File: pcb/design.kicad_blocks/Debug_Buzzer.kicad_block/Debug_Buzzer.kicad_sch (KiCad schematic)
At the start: 5 parts, among them Q1 S8050

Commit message: Rough layout of footprints for `VehicleFlightComputer`.
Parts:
- Q1: footprint Package_TO_SOT_THT:TO-92_Inline -> Package_TO_SOT_SMD:SOT-23_Handsoldering
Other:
- note added: "Debug Buzzer (V6 : SMD Footprint)."
- note removed: "Debug Buzzer (V5 : AST only)."
- moved on the sheet: BZ1, JP2, Q1, R15, R17
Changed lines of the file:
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@@
 	(rectangle
 		(start 461.137 241.681)
-		(end 541.02 284.48)
+		(end 551.18 284.48)
 		(stroke
 			(width 0.8128)
@@
 		)
 	)
-	(text "Debug Buzzer (V5 : AST only)."
+	(text "Debug Buzzer (V6 : SMD Footprint)."
 		(exclude_from_sim no)
 		(at 461.01 240.03 0)
@@
 	)
 	(junction
-		(at 501.65 266.7)
+		(at 506.73 266.7)
 		(diameter 0)
 		(color 0 0 0 0)
@@
 	(wire
 		(pts
-			(xy 501.65 260.35) (xy 499.11 260.35)
-		)
-		(stroke
-			(width 0)
-			(type default)
-		)
-	)
-	(wire
-		(pts
-			(xy 509.27 254) (xy 509.27 251.46)
-		)
-		(stroke
-			(width 0)
-			(type default)
-		)
-	)
-	(wire
-		(pts
-			(xy 491.49 260.35) (xy 488.95 260.35)
-		)
-		(stroke
-			(width 0)
-			(type default)
-		)
-	)
-	(wire
-		(pts
-			(xy 501.65 260.35) (xy 501.65 266.7)
-		)
-		(stroke
-			(width 0)
-			(type default)
-		)
-	)
-	(wire
-		(pts
-			(xy 491.49 273.05) (xy 488.95 273.05)
-		)
-		(stroke
-			(width 0)
-			(type default)
-		)
-	)
-	(wire
-		(pts
-			(xy 501.65 273.05) (xy 499.11 273.05)
-		)
-		(stroke
-			(width 0)
-			(type default)
-		)
-	)
-	(wire
-		(pts
-			(xy 509.27 259.08) (xy 509.27 261.62)
-		)
-		(stroke
-			(width 0)
-			(type default)
-		)
-	)
-	(wire
-		(pts
-			(xy 501.65 266.7) (xy 501.65 273.05)
+			(xy 506.73 260.35) (xy 504.19 260.35)
+		)
+		(stroke
+			(width 0)
+			(type default)
+		)
+	)
+	(wire
+		(pts
+			(xy 514.35 254) (xy 514.35 251.46)
+		)
+		(stroke
+			(width 0)
+			(type default)
+		)
+	)
+	(wire
+		(pts
+			(xy 496.57 260.35) (xy 494.03 260.35)
+		)
+		(stroke
+			(width 0)
+			(type default)
+		)
+	)
+	(wire
+		(pts
+			(xy 506.73 260.35) (xy 506.73 266.7)
+		)
+		(stroke
+			(width 0)
+			(type default)
+		)
+	)
+	(wire
+		(pts
+			(xy 496.57 273.05) (xy 494.03 273.05)
+		)
+		(stroke
+			(width 0)
+			(type default)
+		)
+	)
+	(wire
+		(pts
+			(xy 506.73 273.05) (xy 504.19 273.05)
+		)
+		(stroke
+			(width 0)
+			(type default)
+		)
+	)
+	(wire
+		(pts
+			(xy 514.35 259.08) (xy 514.35 261.62)
+		)
+		(stroke
+			(width 0)
+			(type default)
+		)
+	)
+	(wire
+		(pts
+			(xy 506.73 266.7) (xy 506.73 273.05)
 		)
 		(stroke
@@
 	(global_label "buzzer"
 		(shape bidirectional)
-		(at 485.14 266.7 180)
+		(at 490.22 266.7 180)
 		(fields_autoplaced yes)
 		(effects
@@
 		)
 		(property "Intersheetrefs" "${INTERSHEET_REFS}"
-			(at 474.8145 266.7 0)
+			(at 479.8945 266.7 0)
 			(effects
 				(font
@@
 	(symbol
 		(lib_id "power:GND")
-		(at 509.27 271.78 0)
+		(at 514.35 271.78 0)
 		(unit 1)
 		(exclude_from_sim no)
@@
 		(fields_autoplaced yes)
 		(property "Reference" "#PWR038"
-			(at 509.27 278.13 0)
+			(at 514.35 278.13 0)
 			(effects
 				(font
@@
 		)
 		(property "Value" "GND"
-			(at 509.2701 275.59 90)
+			(at 514.3501 275.59 90)
 			(effects
 				(font
@@
 		)
 		(property "Footprint" ""
-			(at 509.27 271.78 0)
+			(at 514.35 271.78 0)
 			(effects
 				(font
@@
 		)
 		(property "Datasheet" ""
-			(at 509.27 271.78 0)
+			(at 514.35 271.78 0)
 			(effects
 				(font
@@
 		)
 		(property "Description" "Power symbol creates a global label with name \"GND\" , ground"
-			(at 509.27 271.78 0)
+			(at 514.35 271.78 0)
 			(effects
 				(font
@@
 	(symbol
 		(lib_id "Jumper:Jumper_3_Bridged12")
-		(at 488.95 266.7 270)
+		(at 494.03 266.7 270)
 		(mirror x)
 		(unit 1)
@@
 		(fields_autoplaced yes)
 		(property "Reference" "JP2"
-			(at 491.49 266.6999 90)
+			(at 496.57 266.6999 90)
 			(effects
 				(font
@@
 		)
 		(property "Value" "Jumper_3_Bridged12"
-			(at 491.49 267.9699 90)
+			(at 496.57 267.9699 90)
 			(effects
 				(font
@@
 		)
 		(property "Footprint" "Connector_PinHeader_2.54mm:PinHeader_1x03_P2.54mm_Vertical"
-			(at 488.95 266.7 0)
+			(at 494.03 266.7 0)
 			(effects
 				(font
@@
 		)
 		(property "Datasheet" "~"
-			(at 488.95 266.7 0)
+			(at 494.03 266.7 0)
 			(effects
 				(font
@@
 		)
 		(property "Description" "Jumper, 3-pole, pins 1+2 closed/bridged"
-			(at 488.95 266.7 0)
+			(at 494.03 266.7 0)
 			(effects
 				(font
@@
 	(symbol
 		(lib_id "power:+3.3V")
-		(at 509.27 251.46 0)
+		(at 514.35 251.46 0)
 		(unit 1)
 		(exclude_from_sim no)
@@
 		(fields_autoplaced yes)
 		(property "Reference" "#PWR034"
-			(at 509.27 255.27 0)
+			(at 514.35 255.27 0)
 			(effects
 				(font
@@
 		)
 		(property "Value" "+3.3V"
-			(at 509.27 246.38 0)
+			(at 514.35 246.38 0)
 			(effects
 				(font
@@
 		)
 		(property "Footprint" ""
-			(at 509.27 251.46 0)
+			(at 514.35 251.46 0)
 			(effects
 				(font
@@
 		)
 		(property "Datasheet" ""
-			(at 509.27 251.46 0)
+			(at 514.35 251.46 0)
 			(effects
 				(font
@@
 		)
 		(property "Description" "Power symbol creates a global label with name \"+3.3V\""
-			(at 509.27 251.46 0)
+			(at 514.35 251.46 0)
 			(effects
 				(font
@@
 	(symbol
 		(lib_id "Device:R")
-		(at 495.3 260.35 90)
+		(at 500.38 260.35 90)
 		(unit 1)
 		(exclude_from_sim no)
@@
 		(fields_autoplaced yes)
 		(property "Reference" "R15"
-			(at 495.3 254 90)
+			(at 500.38 254 90)
 			(effects
 				(font
@@
 		)
 		(property "Value" "50k"
-			(at 495.3 256.54 90)
+			(at 500.38 256.54 90)
 			(effects
 				(font
@@
 		)
 		(property "Footprint" "Resistor_SMD:R_1206_3216Metric_Pad1.30x1.75mm_HandSolder"
-			(at 495.3 262.128 90)
+			(at 500.38 262.128 90)
 			(effects
 				(font
@@
 		)
 		(property "Datasheet" "~"
-			(at 495.3 260.35 0)
+			(at 500.38 260.35 0)
 			(effects
 				(font
@@
 		)
 		(property "Description" "Resistor"
-			(at 495.3 260.35 0)
+			(at 500.38 260.35 0)
 			(effects
 				(font
@@
 	(symbol
 		(lib_id "Transistor_BJT:S8050")
-		(at 506.73 266.7 0)
+		(at 511.81 266.7 0)
 		(unit 1)
 		(exclude_from_sim no)
@@
 		(fields_autoplaced yes)
 		(property "Reference" "Q1"
-			(at 511.81 265.4299 0)
+			(at 516.89 265.4299 0)
 			(effects
 				(font
@@
 		)
 		(property "Value" "S8050"
-			(at 511.81 267.9699 0)
-			(effects
-				(font
-					(size 1.27 1.27)
-				)
-				(justify left)
-			)
-		)
-		(property "Footprint" "Package_TO_SOT_THT:TO-92_Inline"
-			(at 511.81 268.605 0)
+			(at 516.89 267.9699 0)
+			(effects
+				(font
+					(size 1.27 1.27)
+				)
+				(justify left)
+			)
+		)
+		(property "Footprint" "Package_TO_SOT_SMD:SOT-23_Handsoldering"
+			(at 516.89 268.605 0)
 			(effects
 				(font
@@
 		)
 		(property "Datasheet" "http://www.unisonic.com.tw/datasheet/S8050.pdf"
-			(at 506.73 266.7 0)
+			(at 511.81 266.7 0)
 			(effects
 				(font
@@
 		)
 		(property "Description" "0.7A Ic, 20V Vce, Low Voltage High Current NPN Transistor, TO-92"
-			(at 506.73 266.7 0)
+			(at 511.81 266.7 0)
 			(effects
 				(font
@@
 	(symbol
 		(lib_id "Device:Buzzer")
-		(at 511.81 256.54 0)
+		(at 516.89 256.54 0)
 		(unit 1)
 		(exclude_from_sim no)
@@
 		(dnp no)
 		(property "Reference" "BZ1"
-			(at 515.62 255.2699 0)
+			(at 520.7 255.2699 0)
 			(effects
 				(font
@@
 		)
 		(property "Value" "AST1109MLTRQ"
-			(at 515.62 257.8099 0)
+			(at 520.7 257.8099 0)
 			(effects
 				(font
@@
 		)
 		(property "Footprint" "Buzzer_Beeper:Buzzer_Mallory_AST1109MLTRQ"
-			(at 511.175 254 90)
+			(at 516.255 254 90)
 			(effects
 				(font
@@
 		)
 		(property "Datasheet" "~"
-			(at 511.175 254 90)
+			(at 516.255 254 90)
 			(effects
 				(font
@@
 		)
 		(property "Description" "Buzzer, polarized"
-			(at 511.81 256.54 0)
+			(at 516.89 256.54 0)
 			(effects
 				(font
@@
 	(symbol
 		(lib_id "Device:R")
-		(at 495.3 273.05 90)
+		(at 500.38 273.05 90)
 		(unit 1)
 		(exclude_from_sim no)
@@
 		(dnp no)
 		(property "Reference" "R17"
-			(at 495.3 279.4 90)
+			(at 500.38 279.4 90)
 			(effects
 				(font
@@
 		)
 		(property "Value" "10k"
-			(at 495.3 276.86 90)
+			(at 500.38 276.86 90)
 			(effects
 				(font
@@
 		)
 		(property "Footprint" "Resistor_SMD:R_1206_3216Metric_Pad1.30x1.75mm_HandSolder"
-			(at 495.3 274.828 90)
+			(at 500.38 274.828 90)
 			(effects
 				(font
@@
 		)
 		(property "Datasheet" "~"
-			(at 495.3 273.05 0)
+			(at 500.38 273.05 0)
 			(effects
 				(font
@@
 		)
 		(property "Description" "Resistor"
-			(at 495.3 273.05 0)
-			(effects
-				(font
+			(at 500.38 273.05 0)
+			(effects
+				(font

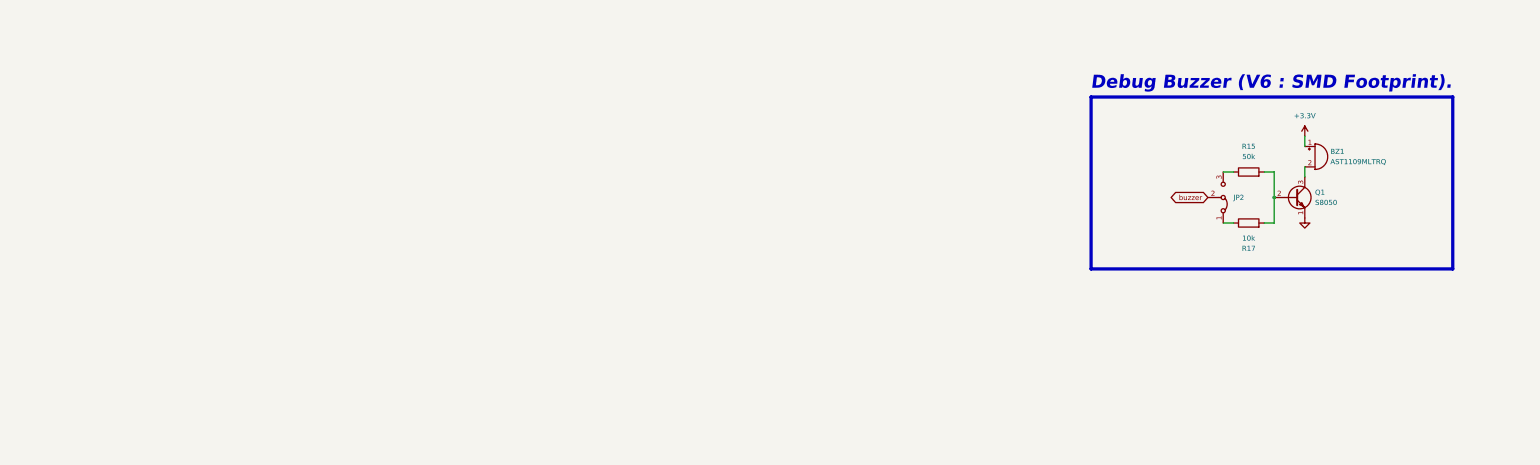
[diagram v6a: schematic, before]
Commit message: Debug buzzer simplified.
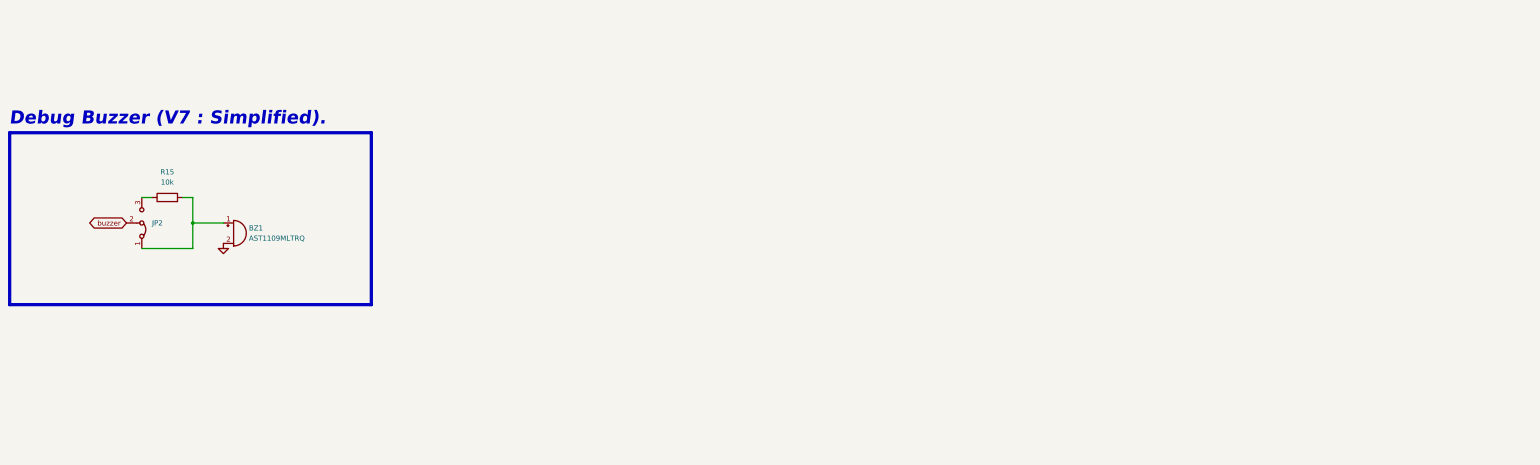
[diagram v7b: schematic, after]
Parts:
- removed Q1: S8050, Package_TO_SOT_SMD:SOT-23_Handsoldering, symbol Transistor_BJT:S8050
- removed R17: 10k, Resistor_SMD:R_1206_3216Metric_Pad1.30x1.75mm_HandSolder, symbol Device:R
- R15: value 50k -> 10k
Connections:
- net +3.3V is gone; now on an unnamed net: BZ1.1 (+)
- net GND: now also BZ1.2 (-)
- net at JP2.1 (A): now also R15.2
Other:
- note added: "Debug Buzzer (V7 : Simplified)."
- note removed: "Debug Buzzer (V6 : SMD Footprint)."
- moved on the sheet: BZ1, JP2, R15
